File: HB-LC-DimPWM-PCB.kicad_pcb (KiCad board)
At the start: 2 copper layers, 167.6 x 57.6 mm, 237 parts, among them J1 SWD, J2 12V Input, J3 Conn_01x05_Male, J4 Conn_01x05_Male, J5 Conn_01x05_Male, J6 Conn_01x05_Male, Q1 S9013, Q10 BSS84, Q11 2N7002, Q12 BSS84, Q13 VS5810AS, Q14 VS5810AS, Q15 VS5810AS, Q16 VS5810AS, Q17 S9013, Q18 S9013, Q19 S9013, Q2 BSS84, Q20 S9013, Q21 BSS84, Q22 2N7002, Q23 BSS84, Q24 2N7002, Q25 BSS84, Q26 2N7002, Q27 BSS84, Q28 2N7002, Q29 VS5810AS, Q3 2N7002, Q30 VS5810AS, Q31 VS5810AS, Q32 VS5810AS, Q33 S9013, Q34 S9013, Q35 S9013, Q36 S9013, Q37 BSS84, Q38 2N7002, Q39 BSS84, Q4 2N7002, Q40 2N7002, Q41 BSS84, Q42 2N7002, Q43 BSS84, Q44 2N7002, Q45 VS5810AS, Q46 VS5810AS, Q47 VS5810AS, Q48 VS5810AS, Q49 S9013, Q5 S9013, Q50 S9013, Q51 S9013, Q52 S9013, Q53 BSS84, Q54 2N7002, Q55 BSS84, Q56 2N7002, Q57 BSS84, Q58 2N7002, Q59 BSS84, Q6 S9013, Q60 2N7002, Q61 VS5810AS, Q62 VS5810AS, Q63 VS5810AS, Q64 VS5810AS, Q7 S9013, Q8 BSS84, Q9 2N7002, U1 STM32F103C8Tx, U2 AMS1117-3.3, U3 HomeMatic-sensor, Y1 8MHz

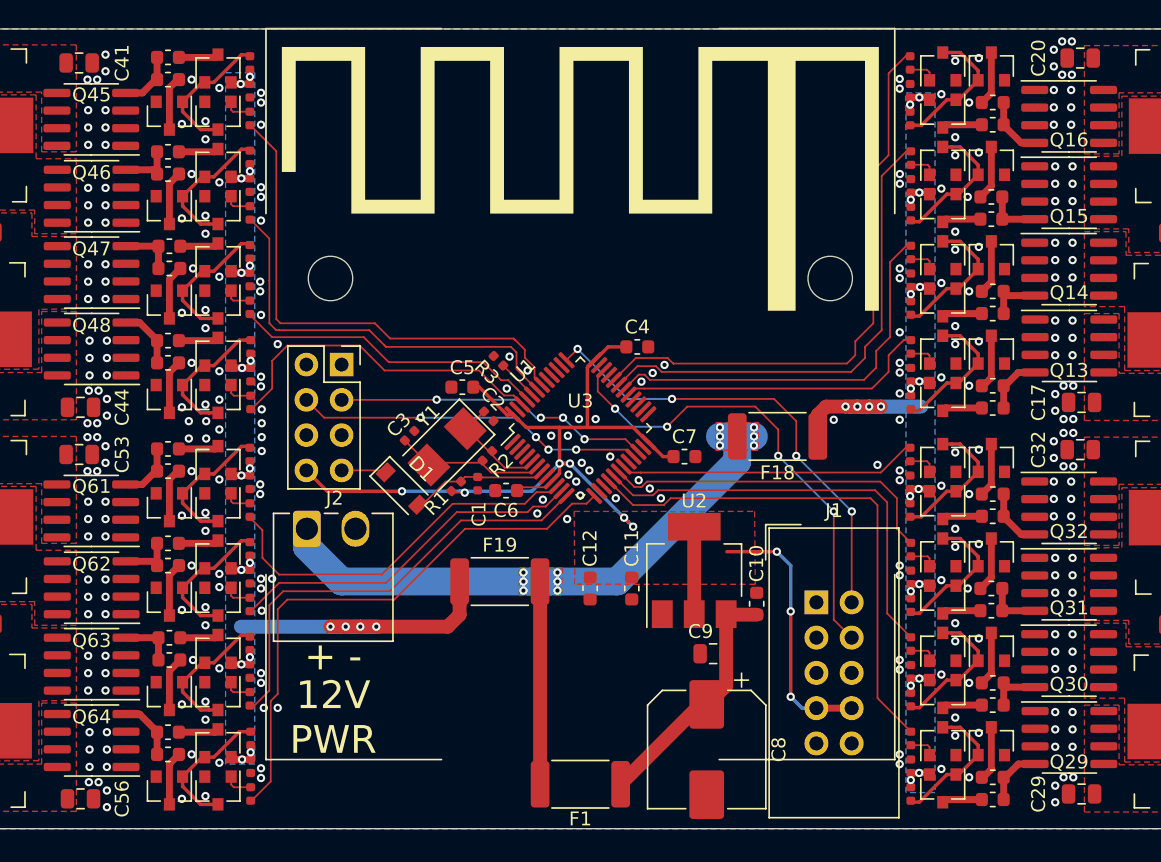
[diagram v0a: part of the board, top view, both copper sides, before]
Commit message: Add tons of manual via stitching
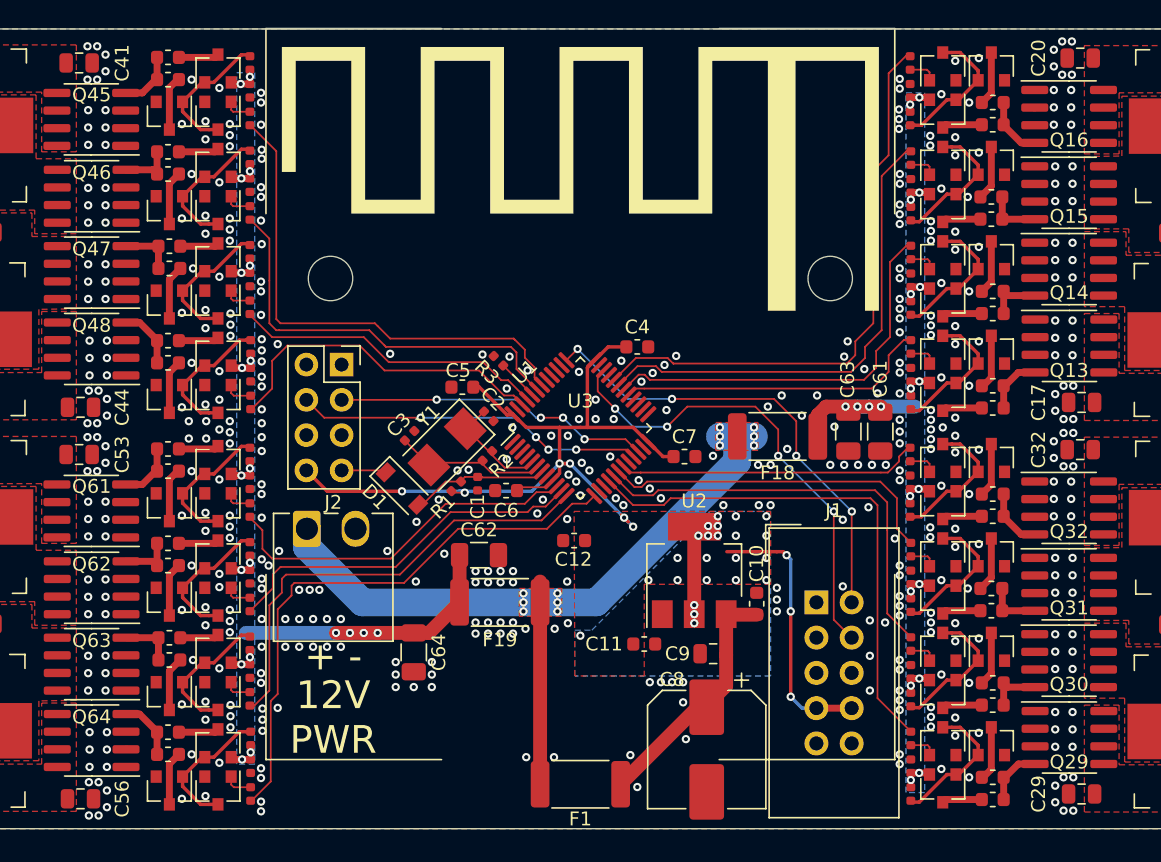
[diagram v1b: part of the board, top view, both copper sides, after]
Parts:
- added C61: 10uF, Capacitor_SMD:C_1206_3216Metric, F.Cu at (194.5, 91.0)
- added C62: 10uF, Capacitor_SMD:C_1206_3216Metric, F.Cu at (165.6, 99.9)
- added C63: 10uF, Capacitor_SMD:C_1206_3216Metric, F.Cu at (192.2, 91.0)
- added C64: 10uF, Capacitor_SMD:C_1206_3216Metric, F.Cu at (160.9, 106.9)
- C8: value 220uF -> 100uF; footprint Capacitor_SMD:CP_Elec_8x10 -> Capacitor_SMD:CP_Elec_8x6.7
- moved C11 4.10 mm to (177.5, 106.3), turned to 0 degrees
- moved C12 3.64 mm to (172.4, 98.8), turned to 180 degrees
- moved F19 1.50 mm to (167.1, 103.3)
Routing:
- net /PWM4: track 27.6 -> 26.3 mm
- net +12V: track 55.8 -> 57.0 mm
- net /PWM5: track 25.9 -> 26.6 mm
- net /Dimmer channel 3/+12V: track 43.0 -> 42.4 mm
- net /PWM6: track 32.7 -> 33.2 mm
- net +3V3: track 86.6 -> 86.9 mm, vias 9 -> 32
- net GND: vias 453 -> 633
- added copper zone on B.Cu, net +3V3

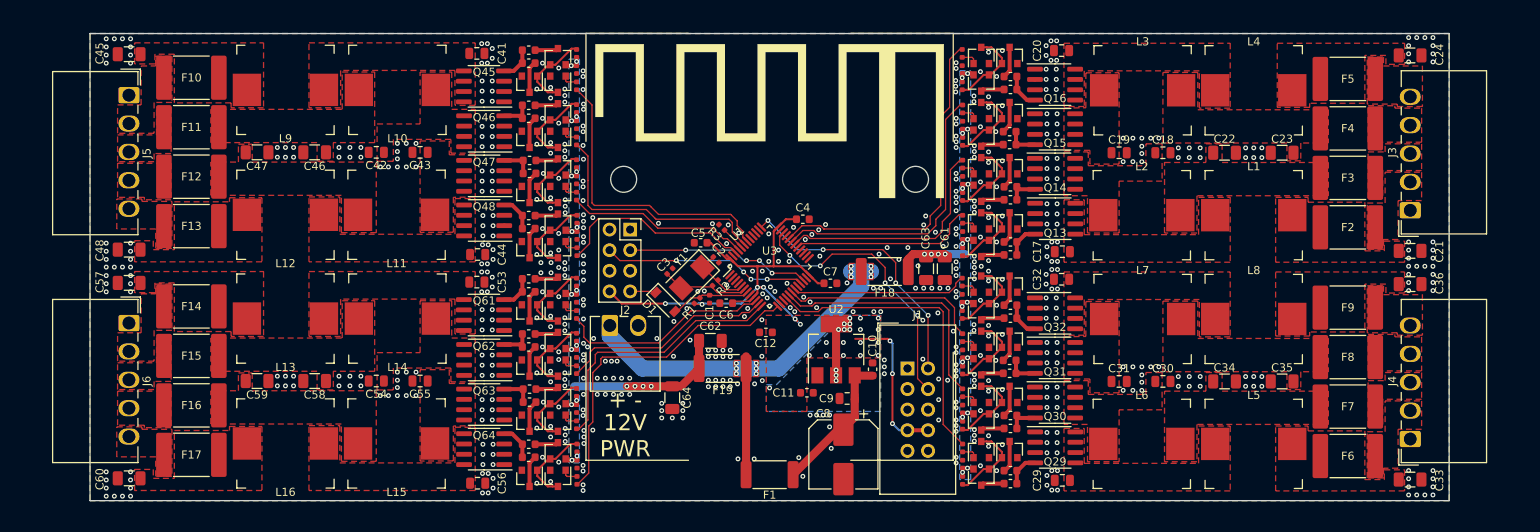
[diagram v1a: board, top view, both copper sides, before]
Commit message: Add pin 1 markers
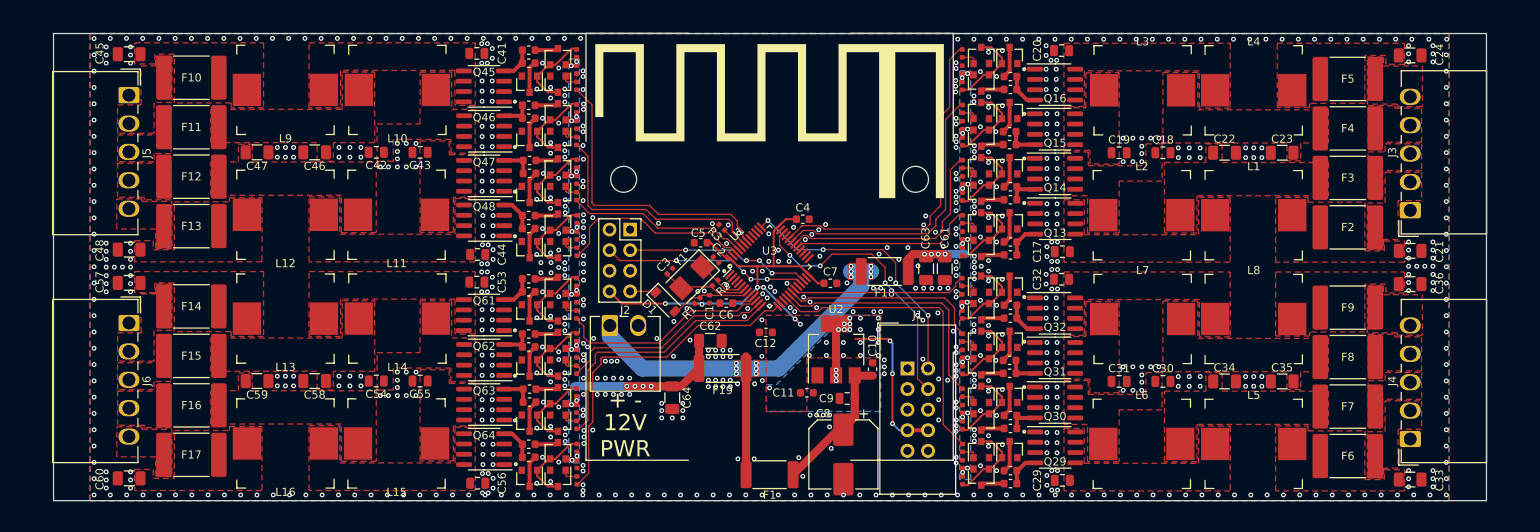
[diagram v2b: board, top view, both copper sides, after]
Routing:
- net GND: vias 633 -> 815
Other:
- board size 167.6 x 57.6 mm -> 176.7 x 57.6 mm

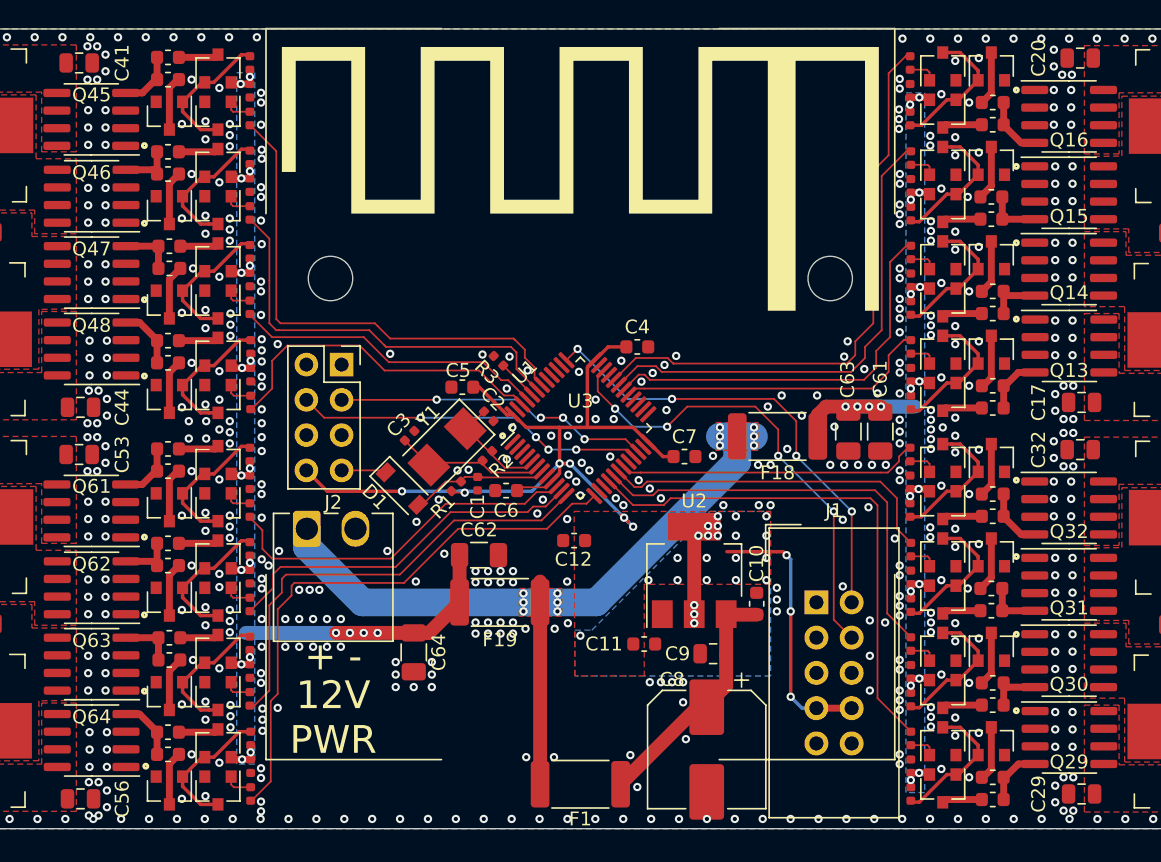
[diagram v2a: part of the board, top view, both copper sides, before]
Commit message: Remove vias too close to one another for safe drilling
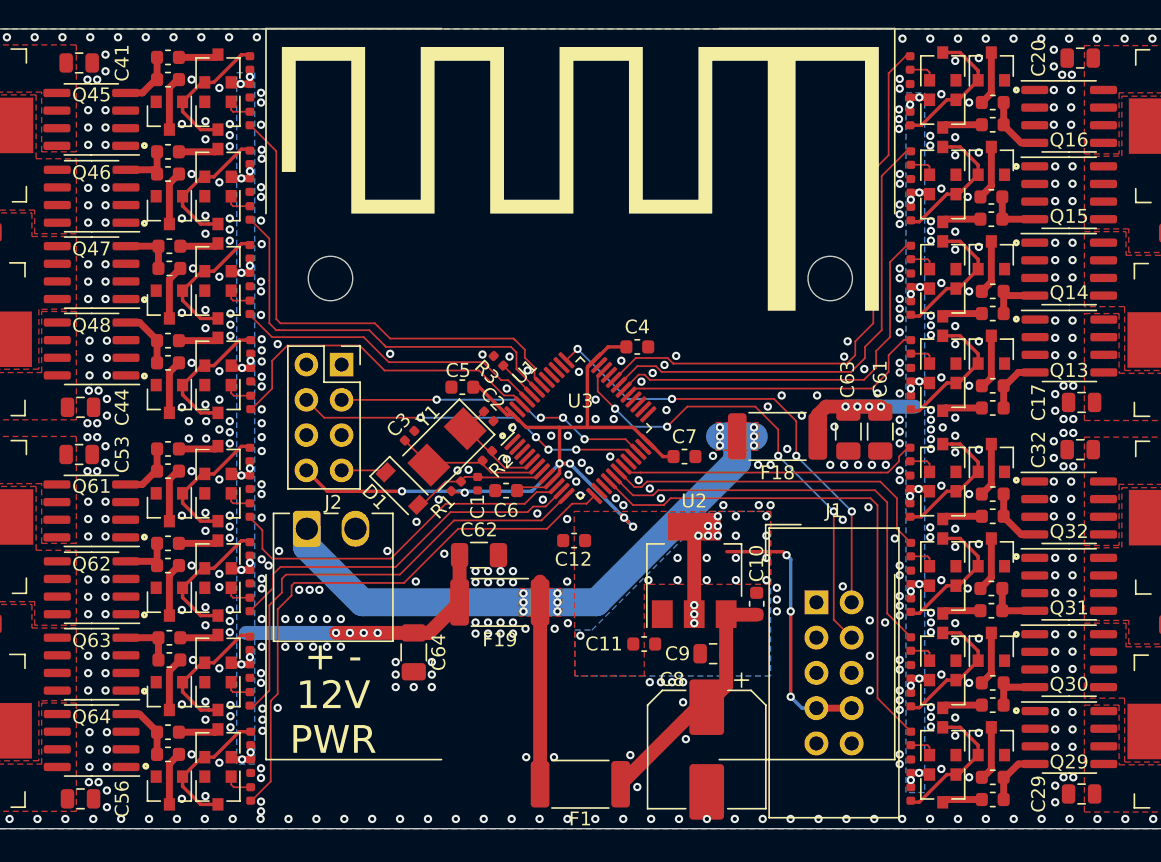
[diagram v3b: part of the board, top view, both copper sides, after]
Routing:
- net GND: vias 815 -> 809
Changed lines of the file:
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@@
     (thickness 1.6)
     (drawings 26)
-    (tracks 1659)
+    (tracks 1653)
     (zones 0)
     (modules 241)
@@
   (via (at 153.65 104.5) (size 0.6) (drill 0.3) (layers F.Cu B.Cu) (net 1))
   (via (at 152.65 104.5) (size 0.6) (drill 0.3) (layers F.Cu B.Cu) (net 1))
-  (via (at 138.1 63.25) (size 0.6) (drill 0.3) (layers F.Cu B.Cu) (net 1))
-  (via (at 137.4 63.25) (size 0.6) (drill 0.3) (layers F.Cu B.Cu) (net 1))
-  (via (at 137.5 118.65) (size 0.6) (drill 0.3) (layers F.Cu B.Cu) (net 1))
-  (via (at 138.2 118.65) (size 0.6) (drill 0.3) (layers F.Cu B.Cu) (net 1))
-  (via (at 208.4 118.3) (size 0.6) (drill 0.3) (layers F.Cu B.Cu) (net 1))
-  (via (at 207.7 118.3) (size 0.6) (drill 0.3) (layers F.Cu B.Cu) (net 1))
   (via (at 167.15 105.55) (size 0.6) (drill 0.3) (layers F.Cu B.Cu) (net 1))
   (via (at 168.05 105.55) (size 0.6) (drill 0.3) (layers F.Cu B.Cu) (net 1))

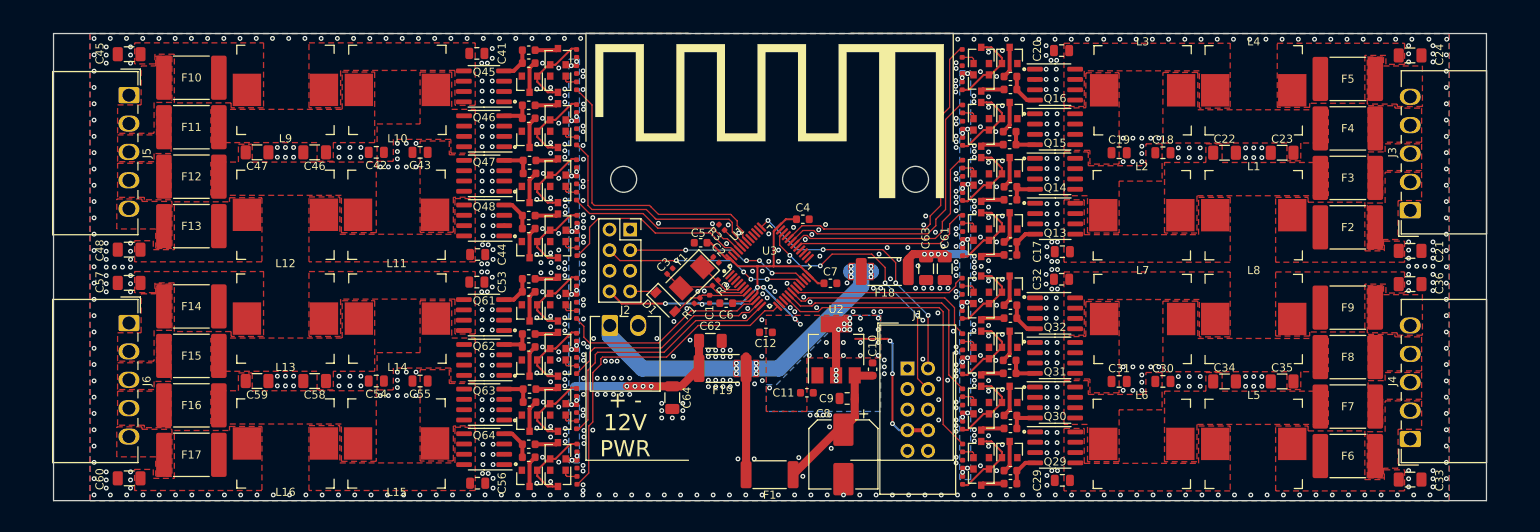
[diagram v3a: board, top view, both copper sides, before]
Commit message: Mark GND pin on lamp connectors
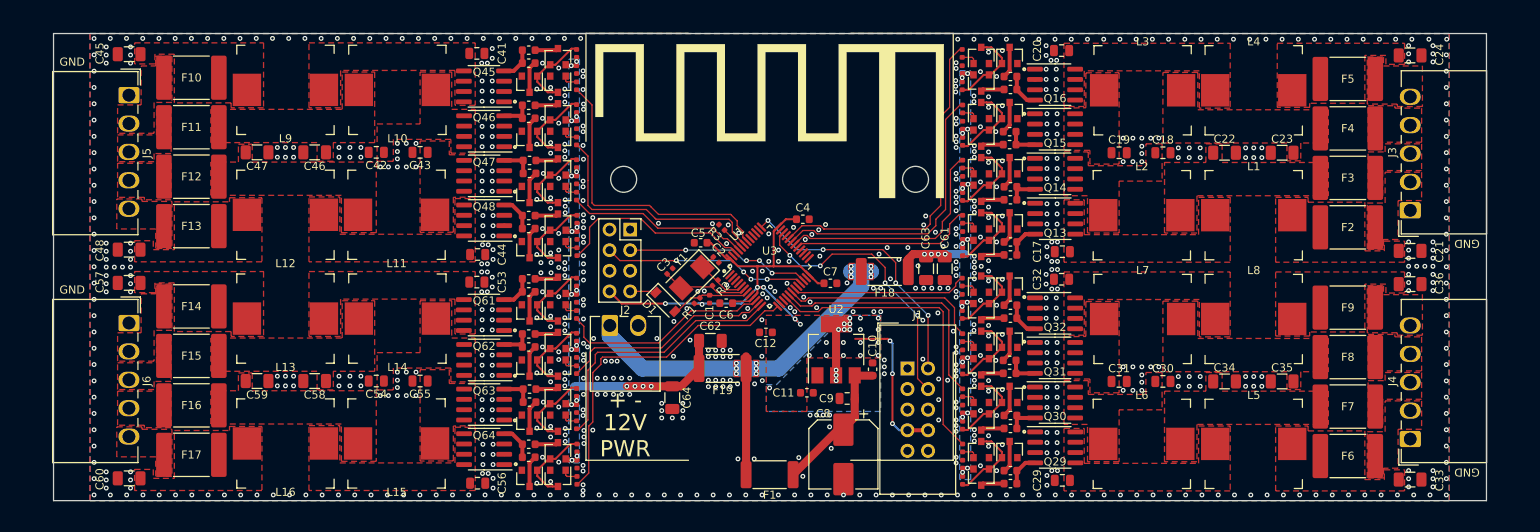
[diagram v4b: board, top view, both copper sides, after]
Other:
- board text added: "GND"
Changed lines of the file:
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@@
   (general
     (thickness 1.6)
-    (drawings 26)
+    (drawings 30)
     (tracks 1653)
     (zones 0)
@@
     )
   )
+  (gr_text GND (at 86.9 93.6) (layer F.SilkS)
+    (effects (font (size 1 1) (thickness 0.15)))
+  )
+  (gr_text GND (at 86.9 65.5) (layer F.SilkS)
+    (effects (font (size 1 1) (thickness 0.15)))
+  )
+  (gr_text GND (at 258.9 87.9 180) (layer F.SilkS)
+    (effects (font (size 1 1) (thickness 0.15)))
+  )
+  (gr_text GND (at 258.9 116.1 180) (layer F.SilkS)
+    (effects (font (size 1 1) (thickness 0.15)))
+  )
   (gr_circle (center 141.5 70.4) (end 141.6 70.4) (layer F.SilkS) (width 0.3))

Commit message: Add revision indicator
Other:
- board text added: "HB PWM dimmer Rev A Tobias Mädel Tobias Schramm 2020"
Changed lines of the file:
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@@
   (general
     (thickness 1.6)
-    (drawings 30)
+    (drawings 31)
     (tracks 1653)
     (zones 0)
@@
     )
   )
+  (gr_text "HB PWM dimmer Rev A\nTobias Mädel\nTobias Schramm 2020" (at 159.6 79.2) (layer F.SilkS)
+    (effects (font (size 1.3 1.3) (thickness 0.2)) (justify left))
+  )
   (gr_text GND (at 86.9 93.6) (layer F.SilkS)
